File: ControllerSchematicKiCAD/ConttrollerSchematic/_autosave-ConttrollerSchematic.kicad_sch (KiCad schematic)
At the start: 8 parts

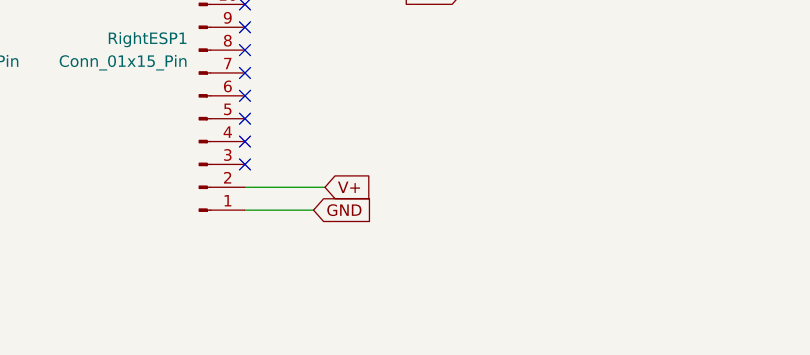
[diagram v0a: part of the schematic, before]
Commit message: imported from 3d model for exact dimensions
I imported the dxf from the model for the controller and then I made that the edge cuts for the board. I also added some art
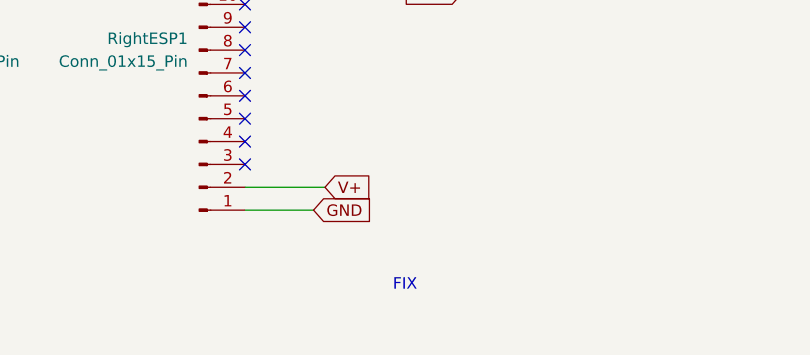
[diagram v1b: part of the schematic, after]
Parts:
- Button12222, Button2: footprint Button_Switch_SMD:SW_Push_1P1T_NO_CK_PTS125Sx73PSMTR -> Button_Switch_SMD:SW_Push_1P1T-SH_NO_CK_KMR2xxG
- Screen1: footprint Connector_PinSocket_2.54mm:PinSocket_1x04_P2.54mm_Vertical -> Connector_PinSocket_1.00mm:PinSocket_1x04_P1.00mm_Vertical
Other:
- note added: "FIX"
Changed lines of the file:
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@@
 	(generator_version "9.0")
 	(paper "A4")
+	(text "FIX\n"
+		(exclude_from_sim no)
+		(at 214.63 103.632 0)
+		(effects
+			(font
+				(size 1.27 1.27)
+			)
+		)
+	)
 	(no_connect
 		(at 196.85 87.63)
@@
 			)
 		)
-		(property "Footprint" "Connector_PinSocket_2.54mm:PinSocket_1x04_P2.54mm_Vertical"
+		(property "Footprint" "Connector_PinSocket_1.00mm:PinSocket_1x04_P1.00mm_Vertical"
 			(at 232.41 66.04 0)
 			(effects
@@
 			)
 		)
-		(property "Footprint" "Button_Switch_SMD:SW_Push_1P1T_NO_CK_PTS125Sx73PSMTR"
+		(property "Footprint" "Button_Switch_SMD:SW_Push_1P1T-SH_NO_CK_KMR2xxG"
 			(at 73.66 85.09 0)
 			(effects
@@
 			)
 		)
-		(property "Footprint" "Button_Switch_SMD:SW_Push_1P1T_NO_CK_PTS125Sx73PSMTR"
+		(property "Footprint" "Button_Switch_SMD:SW_Push_1P1T-SH_NO_CK_KMR2xxG"
 			(at 73.66 68.58 0)
 			(effects
